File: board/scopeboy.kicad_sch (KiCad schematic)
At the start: 49 parts, among them J1 USB_B_Micro, J2 Conn_02x26_Odd_Even, J3 Conn_02x26_Odd_Even, J4 SM03B-SRSS-TB, SW1 SW_Push, SW2 SW_Push, U1 RP2350_80QFN, U2 NCP1117-3.3_SOT223, U3 W25Q128JVS, U4 DNF, Y1 ABM8-272-T3

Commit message: Continued schematic moving from old version to new version
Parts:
- added C23: 10pF, symbol Device:C
- added C24, C44: 1u, Capacitor_SMD:C_0603_1608Metric, symbol Device:C
- added C25: 120p, Capacitor_SMD:C_0603_1608Metric, symbol Device:C
- added C26, C27, C28, C29, C30, C31, C32, C33, C34, C36, C38, C39, C40, C41: 100n, Capacitor_SMD:C_0603_1608Metric, symbol Device:C
- added C35, C37, C42: 22u, Capacitor_SMD:C_0603_1608Metric, symbol Device:C
- added C43, C45, C48, C49, C50: 2.2u, Capacitor_SMD:C_0603_1608Metric, symbol Device:C
- added C46: 10n, Capacitor_SMD:C_0603_1608Metric, symbol Device:C
- added C47: 4.7u, Capacitor_SMD:C_0603_1608Metric, symbol Device:C
- added C51, C52: 10nF, Capacitor_SMD:C_0603_1608Metric, symbol Device:C
- added D1, D2: BAT54WS-G3-08, Diode_SMD:D_0603_1608Metric, symbol Device:D
- added D3: D, Diode_SMD:D_0603_1608Metric, symbol Device:D
- added D5: ESD9B5.0ST5G, Diode_SMD:D_SOD-923, symbol Diode:ESD9B5.0ST5G
- added J5: SM04B-SRSS-TB, Connector_JST:JST_SH_SM04B-SRSS-TB_1x04-1MP_P1.00mm_Horizontal, symbol Connector_Generic:Conn_01x04
- added J5: Conn_01x10, Connector_PinHeader_2.54mm:PinHeader_1x10_P2.54mm_Vertical, symbol Connector_Generic:Conn_01x10
- added J6: SM03B-SRSS-TB, Connector_JST:JST_SH_SM03B-SRSS-TB_1x03-1MP_P1.00mm_Horizontal, symbol Connector_Generic:Conn_01x03
- added J7: 731000105, CONN_73100-0105_MOL, symbol MolexBNC:731000105
- added J8: HDMI_A, Connector_Video:HDMI_A_Molex_208658-1001_Horizontal, symbol Connector:HDMI_A
- added R12, R15 (x2), R16: 100, Resistor_SMD:R_0603_1608Metric, symbol Device:R
- added R12, R14, R17, R23: 1k, Resistor_SMD:R_0603_1608Metric, symbol Device:R
- added R14: 47, Resistor_SMD:R_0603_1608Metric, symbol Device:R
- added R16: 680, Resistor_SMD:R_0603_1608Metric, symbol Device:R
- added R18: 39, Resistor_SMD:R_0603_1608Metric, symbol Device:R
- added R19, R24: 22, Resistor_SMD:R_0603_1608Metric, symbol Device:R
- added R20, R25: 87k, Resistor_SMD:R_0603_1608Metric, symbol Device:R
- added R21: 100, symbol Device:R
- added R22: 1MEG, Resistor_SMD:R_0603_1608Metric, symbol Device:R
- added R26, R27: 50k, Resistor_SMD:R_0603_1608Metric, symbol Device:R
- added R28, R29: 0, Resistor_SMD:R_0603_1608Metric, symbol Device:R
- added R30, R31, R32, R33, R34, R35, R36, R37: 220, Resistor_SMD:R_0603_1608Metric, symbol Device:R
- added R38, R39, R40, R41: 10K, Resistor_SMD:R_0603_1608Metric, symbol Device:R
- added R5: 1M, symbol Device:R
- added SW3: RotaryEncoder_Switch, Footprints:PEC11L4115FS0020, symbol Device:RotaryEncoder_Switch
- added U10: LM4040DBZ-2.0, Package_TO_SOT_SMD:SOT-23, symbol Reference_Voltage:LM4040DBZ-2.0
- added U11: TLV3501, Package_TO_SOT_SMD:SOT-23-6, symbol rpicoscope:TLV3501
- added U12, U8: DAC5571, Package_TO_SOT_SMD:SOT-23-6, symbol rpicoscope:DAC5571
- added U13: TLV271, Package_TO_SOT_SMD:SOT-23-5, symbol rpicoscope:TLV271
- added U14: LM27762, Package_SON:WSON-12-1EP_3x2mm_P0.5mm_EP1x2.65_ThermalVias, symbol Regulator_SwitchedCapacitor:LM27762
- added U5: LMH6629, Package_TO_SOT_SMD:SOT-23-5, symbol rpicoscope:LMH6629
- added U5: OPA354, Package_TO_SOT_SMD:SOT-23-5, symbol rpicoscope:TPH2501
- added U6: OPA820, Package_TO_SOT_SMD:SOT-23-5, symbol rpicoscope:OPA830
- added U6: ADG621, Package_SO:MSOP-10_3x3mm_P0.5mm, symbol rpicoscope:ADG621
- added U7: ADC08100, Package_SO:TSSOP-24_4.4x7.8mm_P0.65mm, symbol rpicoscope:ADC08100
- added U9: LP2985-3.3, Package_TO_SOT_SMD:SOT-23-5, symbol Regulator_Linear:LP2985-3.3
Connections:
- net +3V3: now also C41.2, C42.2, C48.2, R40.2, R41.2, U7.18 (DRVD), U9.5 (VOUT)
- net GND: now also C41.1, C42.1, C44.1, C46.1, C48.1, C51.2, C52.2, J5.1 (Pin_1), J5.1 (Pin_1), J6.2 (Pin_2), J8.11 (CKS), J8.17 (GND), J8.2 (D2S), J8.5 (D1S), J8.8 (D0S), J8.SH, R28.1, R29.1, SW3.C, SW3.S2, U7.17 (DRGND), U7.23 (PD), U9.2 (GND)
- new net: C33.1, R23.1, U10.1 (K), U13.3 (+)
- new net: R19.2, U7.24 (CLK)
- new net: C40.2, U7.9 (VRM)
- new net: C23.1, D1.2 (A), D2.1 (K), D5.1 (A1), R21.2, R5.1, U5.3 (+)
- new net: U6.3 (+), U8.1 (VOUT)
- new net: R14.2, R15.1, R16.2, U5.1
- new net: R12.2, U5.1, U5.3 (+), U5.4 (-)
- new net: R12.1, R16.1, U5.4 (-), U6.1 (S1), U6.7 (S2)
- new net: R16.1, R17.2, R18.1, U6.1
- new net: R15.2, R16.2, U6.4 (-)
- new net: U11.1 (-), U12.1 (VOUT)
- new net: R22.1, U11.3 (+)
- new net: R24.2, U11.5
- new net: C46.2, U9.4 (BP)
- new net: J8.4 (D1+), R32.1
- new net: J8.7 (D0+), R34.1
- new net: J8.3 (D2-), R31.1
- new net: J8.6 (D1-), R33.1
- new net: J7.1, R21.1
- new net: R20.2, R27.2, U14.2 (FB+)
- new net: J8.19 (HPD), R38.1
- new net: C45.1, U14.10 (C+)
- new net: C45.2, U14.9 (C-)
- new net: J8.1 (D2+), R30.1
- new net: R25.2, R26.2, U14.7 (FB-)
- new net: J8.12 (CK-), R37.1
- new net: R14.1, U6.2 (D1)
- new net: R15.1, U6.8 (D2)
- new net: J8.10 (CK+), R36.1
- new net: J8.9 (D0-), R35.1
- new net: C47.1, U14.5 (CP)
- new net +3.3VA: C24.1, C26.1, C27.2, C28.1, C29.1, C30.1, C31.1, C32.2, C34.1, C35.2, C36.2, C37.2, C38.2, C39.2, C49.1, D1.1 (K), R20.1, R23.2, U11.4, U12.3 (VDD), U12.6 (A0), U13.5, U14.11 (OUT+), U5.5, U5.5, U6.10 (VDD), U6.5, U7.1 (VA), U7.12 (VA), U7.4 (VA), U8.3 (VDD)
- new net +3V3Pico: J5.2 (Pin_2), J5.2 (Pin_2)
- new net +5V: J8.18 (+5V), R38.2, R39.1, R39.2
- new net -3V3: C26.2, C27.1, C28.2, C29.2, C50.1, D3.2 (A), R12.1, R14.1, R17.1, R25.1, U14.6 (OUT-), U5.2, U5.2, U6.2, U6.5 (VSS)
- new net BACKLIGHT: J5.10 (Pin_10)
- new net CHASSIS: D5.2 (A2), J7.2 (GND)
- new net CLK: R19.1
- new net D0: U7.22 (D0)
- new net D1: U7.21 (D1)
- new net D2: U7.20 (D2)
- new net D3: U7.19 (D3)
- new net D4: U7.16 (D4)
- new net D5: U7.15 (D5)
- new net D6: U7.14 (D6)
- new net D7: U7.13 (D7)
- new net D/C: J5.3 (Pin_3)
- new net GNDA: C23.2, C24.2, C25.2, C30.2, C31.2, C32.1, C33.2, C34.2, C35.1, C36.1, C37.1, C38.1, C39.1, C40.1, C43.2, C47.2, C49.2, C50.2, D2.2 (A), R12.2, R14.2, R15.2, R26.1, R27.1, R28.2, R29.2, R5.2, U10.2 (A), U11.2, U11.6, U12.2 (GND), U13.2, U14.1 (PGOOD), U14.13 (PAD), U14.4 (GND), U6.4 (GND), U7.10 (VRB), U7.11 (AGND), U7.2 (AGND), U7.5 (AGND), U7.7 (VIN_GND), U7.8 (AGND), U8.2 (GND), U8.6 (A0)
- new net LCDCS: J5.6 (Pin_6)
- new net MISO: J5.8 (Pin_8)
- new net MOSI: J5.7 (Pin_7)
- new net RESET: J5.4 (Pin_4)
- new net ROTCLK: C51.1, R40.1, SW3.A
- new net ROTDT: C52.1, R41.1, SW3.B
- new net ROTSW: SW3.S1
- new net RX: J6.1 (Pin_1)
- new net SCK: J5.9 (Pin_9)
- new net SCL: J5.3 (Pin_3), U12.4 (SDA), U8.4 (SDA)
- new net SDA: J5.4 (Pin_4), U12.5 (SCL), U8.5 (SCL)
- new net SDCS: J5.5 (Pin_5)
- new net SEL0: U6.9 (IN1)
- new net SEL1: U6.3 (IN2)
- new net TRIG: R24.1
- new net TX: J6.3 (Pin_3)
- new net VIN: C25.1, D3.1 (K), R18.2, R22.2, U7.6 (VIN)
- new net VREF: U13.1, U13.4 (-), U7.3 (VRT)
- new net VSYS: C43.1, C44.2, U14.12 (EN+), U14.3 (VIN), U14.8 (EN-), U9.1 (VIN), U9.3 (ON/~{OFF})
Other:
- note added: "ADC"
- note added: "Analog Front End"
- note added: "CH1"
- note added: "DAC"
- note added: "GAIN"
- note added: "HDMI"
- note added: "HIGH-Z"
- note added: "Joystick Connector"
- note added: "No need for these I think since we are only doing output"
- note added: "OFSET"
- note added: "PSU ANA."
- note added: "PSU DIG."
- note added: "REF"
- note added: "Rotary Encoder"
- note added: "SWITCH"
- note added: "TFT"
- note added: "TODO get this checked by an expert Especially with the updated 1M at the front for the scope probe And the chassis diode"
- note added: "TODO maybe delete this because we might use the 2354B. Or swap to using PSRAM"
- note added: "TODO this might need to be updated to work off of battery"
- note added: "TODO this needs to be updated as well. I think I now have 2 digital power units with the analog side as well"
- note added: "TRIG"
- note added: "UART"
- note added: "Updated these R&C values, should be checked"
- note removed: "TODO maybe delete this because we might use the 2354B"
- company: Raspberry Pi Ltd -> Cornell University Electrical and Computer Engineering
- title: RP2350B QFN80 Minimal Design Example -> Scopeboy
- moved on the sheet: C19, H1, H2, H3, H4, J2, J3

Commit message: Fixed MFR label and added more TOOD
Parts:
- U6: MFR. Part # (none) -> OPA830IDBVR; MRF. Part # OPA830IDBVR -> (none)
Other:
- note added: "TODO do we need to connect the 5V for HDMI?"

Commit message: More TODO notes and swaped ref op amp
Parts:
- U13: value TLV271 -> TLV9101; LCSC Part # C181500 -> C4368903; MRF. Part # (none) -> TLV9101IDBVR
- U7: value ADC08100 -> ADC08060; LCSC Part # C701581 -> C701580; MRF. Part # (none) -> ADC08060CIMTX/NOPB
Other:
- note added: "TODO add attenuation after stage 1 and before stage 2 Also change gain stage so gain is over 10 V/V and fixed since that is the input stable range"
- note added: "TODO double check the diodes"
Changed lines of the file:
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@@
 		)
 	)
+	(text "TODO double check the diodes"
+		(exclude_from_sim no)
+		(at 107.188 334.264 0)
+		(effects
+			(font
+				(size 1.27 1.27)
+			)
+		)
+	)
 	(text "IOs"
 		(exclude_from_sim no)
@@
 		)
 	)
+	(text "TODO add attenuation after \nstage 1 and before stage 2\nAlso change gain stage so\ngain is over 10 V/V and fixed\nsince that is the input stable range"
+		(exclude_from_sim no)
+		(at 167.132 381.762 0)
+		(effects
+			(font
+				(size 1.27 1.27)
+			)
+		)
+	)
 	(text "ADC"
 		(exclude_from_sim no)
@@
 			)
 		)
-		(property "Value" "ADC08100"
+		(property "Value" "ADC08060"
 			(at 468.63 292.7604 0)
 			(effects
@@
 			)
 		)
-		(property "LCSC Part #" "C701581"
+		(property "LCSC Part #" "C701580"
 			(at 455.93 294.64 0)
 			(effects
@@
 			)
 		)
-		(property "MRF. Part #" ""
+		(property "MRF. Part #" "ADC08060CIMTX/NOPB"
 			(at 455.93 294.64 0)
 			(effects
@@
 			)
 		)
-		(property "Value" "TLV271"
+		(property "Value" "TLV9101"
 			(at 358.14 309.88 0)
 			(effects
@@
 			)
 		)
-		(property "LCSC Part #" "C181500"
+		(property "LCSC Part #" "C4368903"
 			(at 350.52 299.72 0)
 			(effects
@@
 			)
 		)
-		(property "MRF. Part #" ""
+		(property "MRF. Part #" "TLV9101IDBVR"
 			(at 350.52 299.72 0)
 			(effects

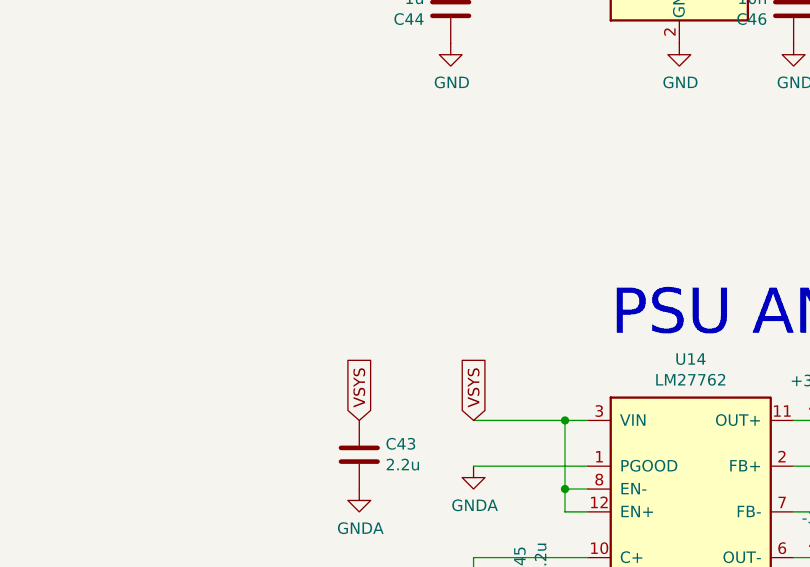
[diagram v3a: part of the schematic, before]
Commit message: Added TODO for 5V charge pump
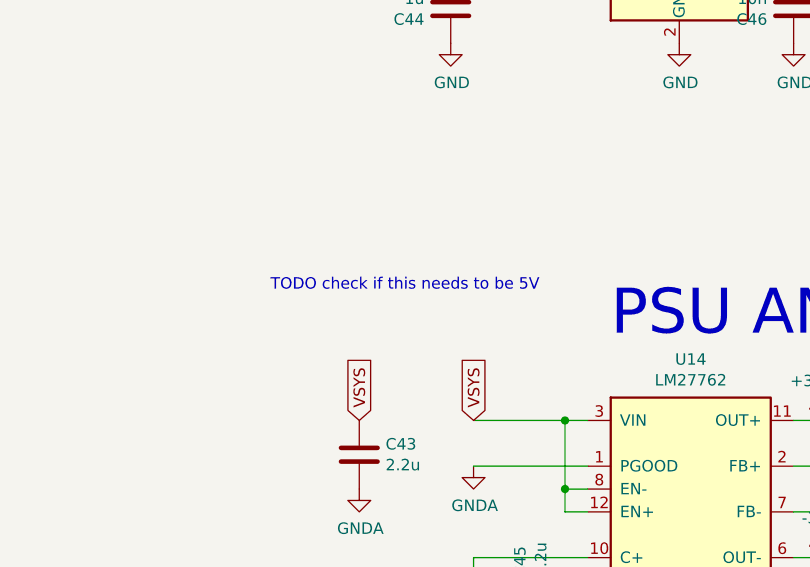
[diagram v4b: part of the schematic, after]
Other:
- note added: "TODO check if this needs to be 5V"
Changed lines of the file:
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@@
+		)
+	)
+	(text "TODO check if this needs to be 5V"
+		(exclude_from_sim no)
+		(at 424.18 221.234 0)
+		(effects
+			(font
+				(size 1.27 1.27)
+			)
 		)
 	)

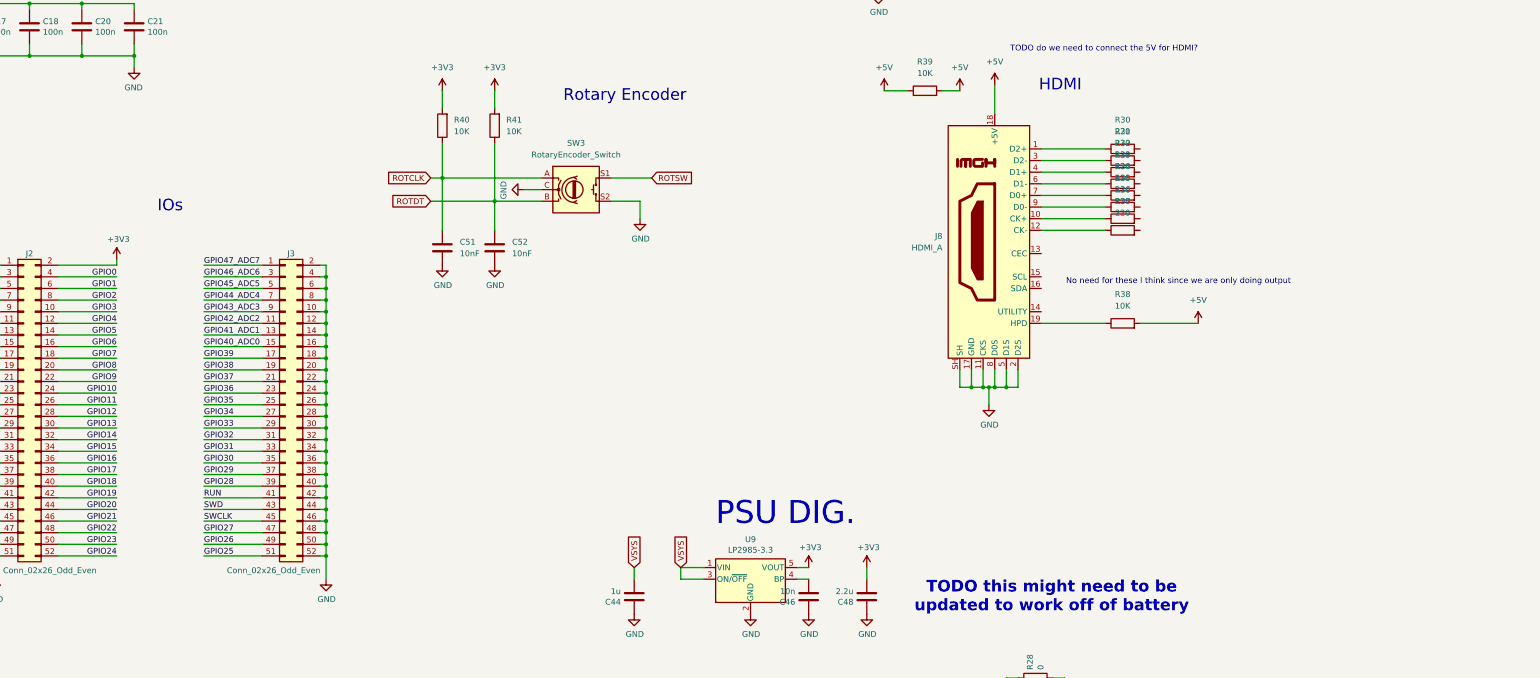
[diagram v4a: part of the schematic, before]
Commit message: HDMI to HSTX GPIO pins, and more TODOs
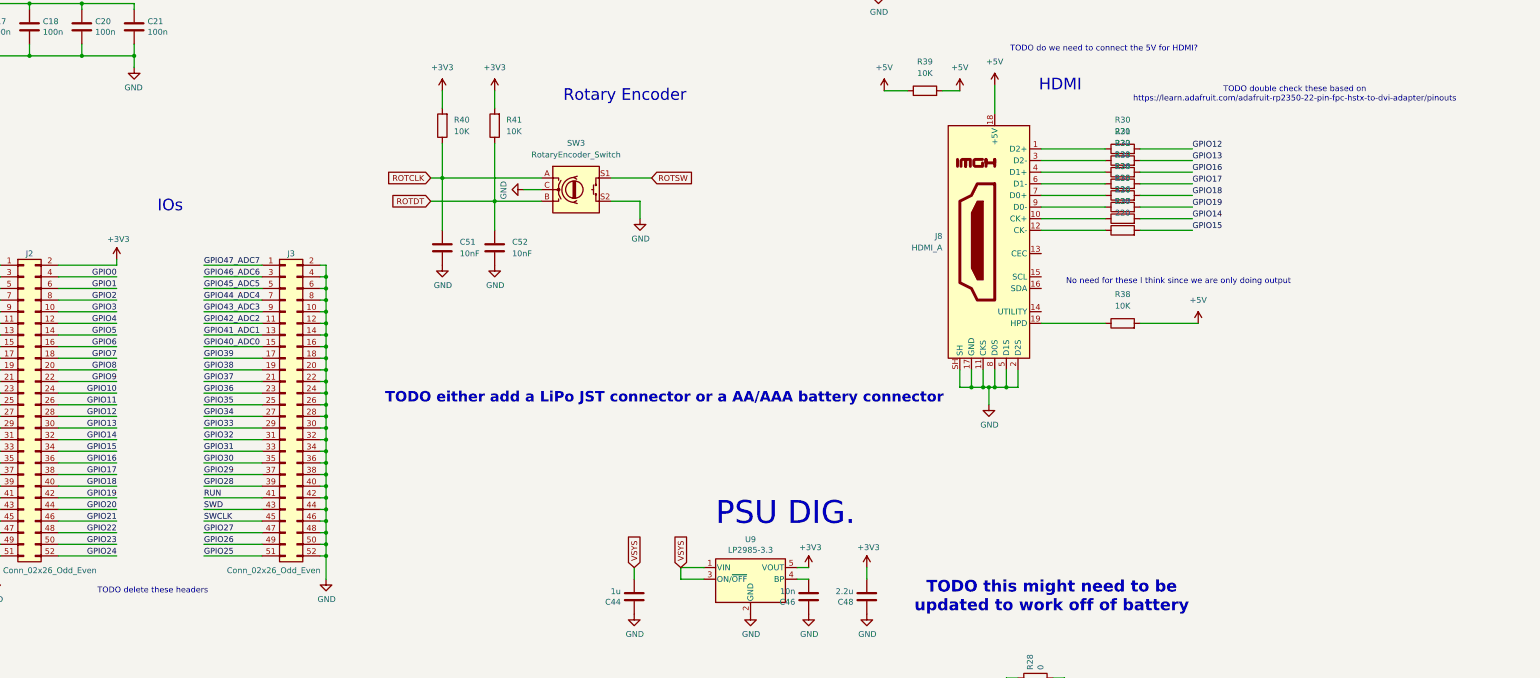
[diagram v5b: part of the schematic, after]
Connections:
- net GPIO12: now also R30.2
- net GPIO13: now also R31.2
- net GPIO14: now also R36.2
- net GPIO15: now also R37.2
- net GPIO16: now also R32.2
- net GPIO17: now also R33.2
- net GPIO18: now also R34.2
- net GPIO19: now also R35.2
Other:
- note added: "TODO delete these headers"
- note added: "TODO double check these based on https://learn.adafruit.com/adafruit-rp2350-22-pin-fpc-hstx-to-dvi-adapter/pinouts"
- note added: "TODO either add a LiPo JST connector or a AA/AAA battery connector"
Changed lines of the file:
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@@
 		)
 	)
+	(text "TODO double check these based on\nhttps://learn.adafruit.com/adafruit-rp2350-22-pin-fpc-hstx-to-dvi-adapter/pinouts"
+		(exclude_from_sim no)
+		(at 573.532 80.772 0)
+		(effects
+			(font
+				(size 1.27 1.27)
+			)
+		)
+	)
 	(text "TODO get this checked by an expert\nEspecially with the updated 1M\nat the front for the scope probe\nAnd the chassis diode"
 		(exclude_from_sim no)
@@
 		)
 	)
+	(text "TODO delete these headers"
+		(exclude_from_sim no)
+		(at 324.104 189.23 0)
+		(effects
+			(font
+				(size 1.27 1.27)
+			)
+		)
+	)
 	(text "TODO add attenuation after \nstage 1 and before stage 2\nAlso change gain stage so\ngain is over 10 V/V and fixed\nsince that is the input stable range"
 		(exclude_from_sim no)
@@
 		)
 	)
+	(text "TODO either add a LiPo JST connector or a AA/AAA battery connector"
+		(exclude_from_sim no)
+		(at 435.864 147.066 0)
+		(effects
+			(font
+				(size 2.286 2.286)
+				(thickness 0.508)
+				(bold yes)
+			)
+		)
+	)
 	(text "No need for these I think since we are only doing output"
 		(exclude_from_sim no)
@@
 	(wire
 		(pts
+			(xy 539.75 100.33) (xy 551.18 100.33)
+		)
+		(stroke
+			(width 0)
+			(type default)
+		)
+	)
+	(wire
+		(pts
 			(xy 335.28 168.91) (xy 347.98 168.91)
 		)
@@
 	(wire
 		(pts
+			(xy 539.75 102.87) (xy 551.18 102.87)
+		)
+		(stroke
+			(width 0)
+			(type default)
+		)
+	)
+	(wire
+		(pts
 			(xy 201.93 93.98) (xy 201.93 81.28)
 		)
@@
 	(wire
 		(pts
+			(xy 539.75 92.71) (xy 551.18 92.71)
+		)
+		(stroke
+			(width 0)
+			(type default)
+		)
+	)
+	(wire
+		(pts
 			(xy 143.51 62.23) (xy 143.51 60.96)
 		)
@@
 	(wire
 		(pts
+			(xy 539.75 97.79) (xy 551.18 97.79)
+		)
+		(stroke
+			(width 0)
+			(type default)
+		)
+	)
+	(wire
+		(pts
 			(xy 234.95 203.2) (xy 250.19 203.2)
 		)
@@
 	(wire
 		(pts
+			(xy 539.75 107.95) (xy 551.18 107.95)
+		)
+		(stroke
+			(width 0)
+			(type default)
+		)
+	)
+	(wire
+		(pts
 			(xy 431.8 251.46) (xy 431.8 256.54)
 		)
@@
 	(wire
 		(pts
+			(xy 539.75 95.25) (xy 551.18 95.25)
+		)
+		(stroke
+			(width 0)
+			(type default)
+		)
+	)
+	(wire
+		(pts
 			(xy 387.35 80.01) (xy 387.35 83.82)
 		)
@@
 	(wire
 		(pts
+			(xy 539.75 105.41) (xy 551.18 105.41)
+		)
+		(stroke
+			(width 0)
+			(type default)
+		)
+	)
+	(wire
+		(pts
 			(xy 387.35 91.44) (xy 387.35 99.06)
 		)
@@
 	(wire
 		(pts
+			(xy 539.75 110.49) (xy 551.18 110.49)
+		)
+		(stroke
+			(width 0)
+			(type default)
+		)
+	)
+	(wire
+		(pts
 			(xy 303.53 179.07) (xy 316.23 179.07)
 		)
@@
 		)
 	)
+	(label "GPIO13"
+		(at 551.18 95.25 0)
+		(effects
+			(font
+				(size 1.27 1.27)
+			)
+			(justify left bottom)
+		)
+	)
 	(label "GPIO32"
 		(at 250.19 193.04 180)
@@
 		)
 	)
+	(label "GPIO14"
+		(at 551.18 107.95 0)
+		(effects
+			(font
+				(size 1.27 1.27)
+			)
+			(justify left bottom)
+		)
+	)
 	(label "GPIO0"
 		(at 18.415 116.205 0)
@@
 		)
 	)
+	(label "GPIO15"
+		(at 551.18 110.49 0)
+		(effects
+			(font
+				(size 1.27 1.27)
+			)
+			(justify left bottom)
+		)
+	)
+	(label "GPIO18"
+		(at 551.18 102.87 0)
+		(effects
+			(font
+				(size 1.27 1.27)
+			)
+			(justify left bottom)
+		)
+	)
 	(label "GPIO21"
 		(at 316.23 173.99 180)
@@
 		)
 	)
+	(label "GPIO12"
+		(at 551.18 92.71 0)
+		(effects
+			(font
+				(size 1.27 1.27)
+			)
+			(justify left bottom)
+		)
+	)
 	(label "GPIO38"
 		(at 250.19 208.28 180)
@@
 		)
 	)
+	(label "GPIO16"
+		(at 551.18 97.79 0)
+		(effects
+			(font
+				(size 1.27 1.27)
+			)
+			(justify left bottom)
+		)
+	)
 	(label "GPIO34"
 		(at 250.19 198.12 180)
@@
 		)
 	)
+	(label "GPIO17"
+		(at 551.18 100.33 0)
+		(effects
+			(font
+				(size 1.27 1.27)
+			)
+			(justify left bottom)
+		)
+	)
 	(label "GPIO2"
 		(at 316.23 125.73 180)
@@
 		(effects
 			(font
+				(size 1.27 1.27)
+			)
+			(justify left bottom)
+		)
+	)
+	(label "GPIO19"
+		(at 551.18 105.41 0)
+		(effects
+			(font

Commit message: Working on simulation for front end
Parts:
- removed C23: 10pF, symbol Device:C
- removed C24: 1u, Capacitor_SMD:C_0603_1608Metric, symbol Device:C
- removed C25: 120p, Capacitor_SMD:C_0603_1608Metric, symbol Device:C
- removed C26, C27, C28, C29, C30, C31, C32, C33, C34: 100n, Capacitor_SMD:C_0603_1608Metric, symbol Device:C
- removed D1, D2: BAT54WS-G3-08, Diode_SMD:D_0603_1608Metric, symbol Device:D
- removed D3: D, Diode_SMD:D_0603_1608Metric, symbol Device:D
- removed D5: ESD9B5.0ST5G, Diode_SMD:D_SOD-923, symbol Diode:ESD9B5.0ST5G
- removed J7: 731000105, CONN_73100-0105_MOL, symbol MolexBNC:731000105
- removed R12, R15 (x2), R16: 100, Resistor_SMD:R_0603_1608Metric, symbol Device:R
- removed R12, R14, R17, R23: 1k, Resistor_SMD:R_0603_1608Metric, symbol Device:R
- removed R14: 47, Resistor_SMD:R_0603_1608Metric, symbol Device:R
- removed R16: 680, Resistor_SMD:R_0603_1608Metric, symbol Device:R
- removed R18: 39, Resistor_SMD:R_0603_1608Metric, symbol Device:R
- removed R21: 100, symbol Device:R
- removed R22: 1MEG, Resistor_SMD:R_0603_1608Metric, symbol Device:R
- removed R24: 22, Resistor_SMD:R_0603_1608Metric, symbol Device:R
- removed R5: 1M, symbol Device:R
- removed U10: LM4040DBZ-2.0, Package_TO_SOT_SMD:SOT-23, symbol Reference_Voltage:LM4040DBZ-2.0
- removed U11: TLV3501, Package_TO_SOT_SMD:SOT-23-6, symbol rpicoscope:TLV3501
- removed U12, U8: DAC5571, Package_TO_SOT_SMD:SOT-23-6, symbol rpicoscope:DAC5571
- removed U13: TLV9101, Package_TO_SOT_SMD:SOT-23-5, symbol rpicoscope:TLV271
- removed U5: LMH6629, Package_TO_SOT_SMD:SOT-23-5, symbol rpicoscope:LMH6629
- removed U5: OPA354, Package_TO_SOT_SMD:SOT-23-5, symbol rpicoscope:TPH2501
- removed U6: OPA820, Package_TO_SOT_SMD:SOT-23-5, symbol rpicoscope:OPA830
- removed U6: ADG621, Package_SO:MSOP-10_3x3mm_P0.5mm, symbol rpicoscope:ADG621
- renumbered C9 to C10, C10 to C11, C11 to C12, C12 to C13, C13 to C14, C14 to C15, C15 to C16, C19 to C17, C16 to C18, C17 to C19, C18 to C20, C20 to C21, C21 to C22, C51 to C23, C52 to C24, C35 to C25, C43 to C26, C36 to C27, C37 to C28, C44 to C29, C22 to C3, C45 to C30, C38 to C31, C39 to C32, C40 to C33, C46 to C34, C47 to C35, C41 to C36, C48 to C37, C42 to C38, C49 to C39, C3 to C4, C50 to C40, C4 to C5, C5 to C6, C6 to C7, C7 to C8, C8 to C9, J6 to J3, J3 to J5, J5 to J6, J5 to J7, R9 to R1, R7 to R10, R8 to R11, R40 to R12, R41 to R13, R20 to R14, R25 to R15, R26 to R16, R39 to R17, R19 to R18, R27 to R19, R10 to R2, R28 to R20, R29 to R21, R30 to R22, R31 to R23, R32 to R24, R33 to R25, R34 to R26, R35 to R27, R36 to R28, R37 to R29, R11 to R3, R38 to R30, R1 to R4, R13 to R5, R4 to R6, R2 to R7, R3 to R8, R6 to R9, U3 to U1, U4 to U2, U2 to U3, U1 to U4, U9 to U5, U14 to U6
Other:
- added sheet Analog Front End (analog_front_end.kicad_sch)
- note added: "TODO place trig on pico"
- note removed: "Analog Front End"
- note removed: "CH1"
- note removed: "DAC"
- note removed: "GAIN"
- note removed: "HIGH-Z"
- note removed: "OFSET"
- note removed: "REF"
- note removed: "SWITCH"
- note removed: "TODO add attenuation after stage 1 and before stage 2 Also change gain stage so gain is over 10 V/V and fixed since that is the input stable range"
- note removed: "TODO double check the diodes"
- note removed: "TODO get this checked by an expert Especially with the updated 1M at the front for the scope probe And the chassis diode"
- note removed: "TRIG"
- note removed: "Updated these R&C values, should be checked"
